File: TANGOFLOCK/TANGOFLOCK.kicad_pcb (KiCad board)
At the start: 2 copper layers, 31.8 x 31.8 mm, 7 parts, among them J1 USB-DEVICE-SHIELD, J2 USB-DEVICE-SHIELD, P2 ANTENNA, Q1 MOSFET_N

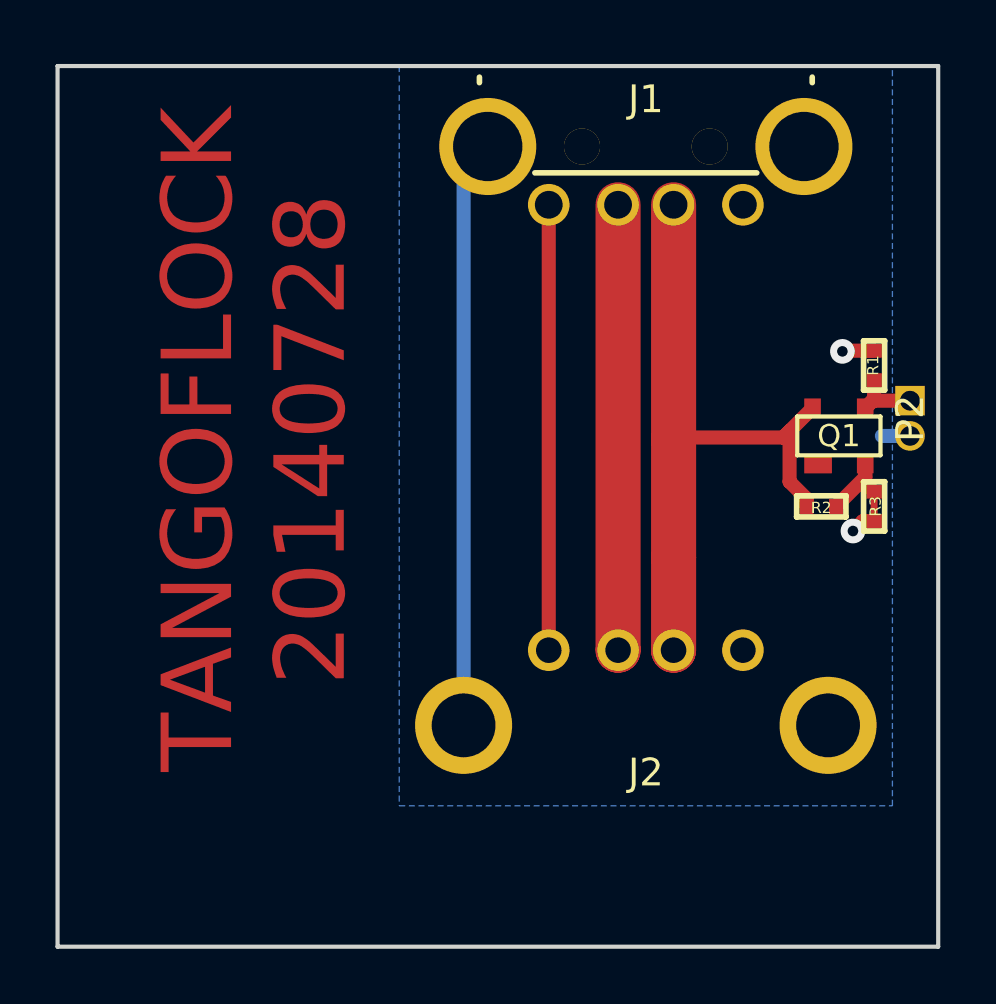
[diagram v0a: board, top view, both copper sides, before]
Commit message: simplified TANGOFLOCK
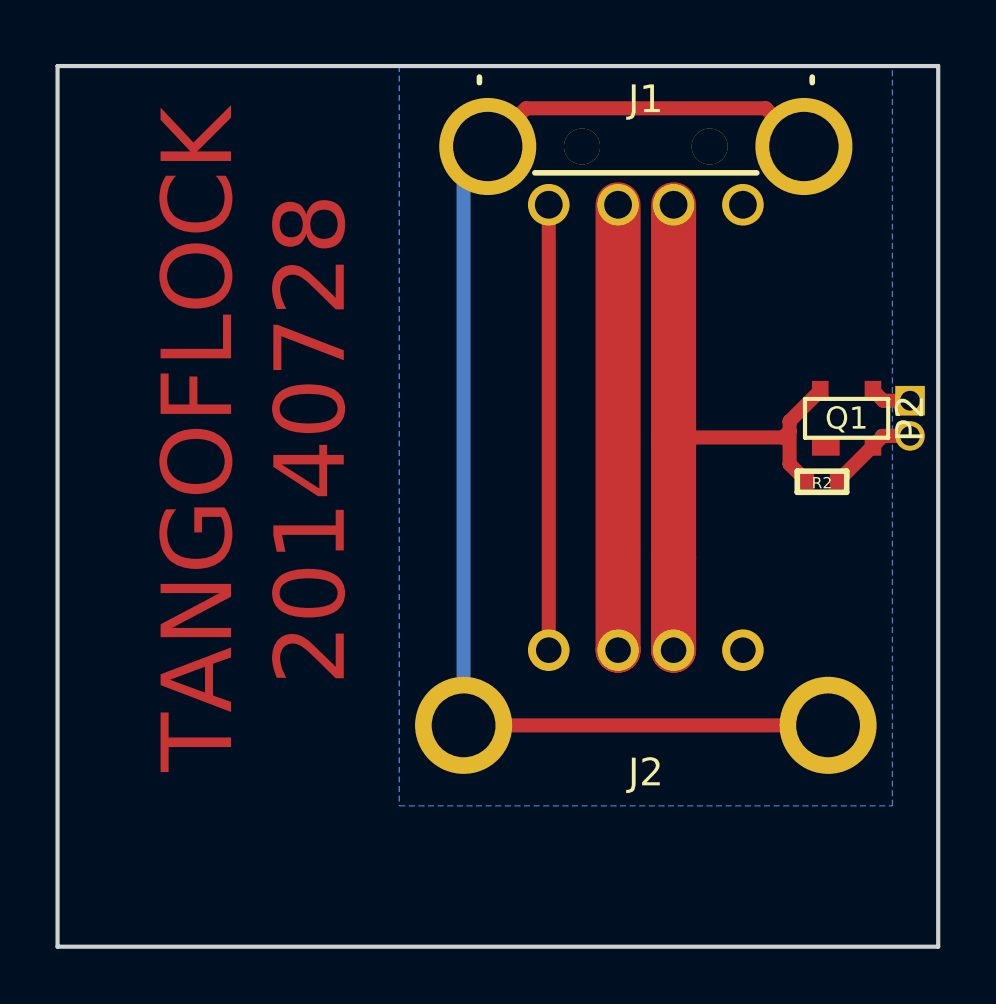
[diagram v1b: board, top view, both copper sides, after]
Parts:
- removed R1: DNP, GSG-0402
- removed R3: 0, GSG-0402-SHORT-10MIL
- moved R2 0.89 mm to (103.8, 91.2)
- moved Q1 0.69 mm to (104.6, 88.9)
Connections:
- Q1 pad S: /SOURCE -> GND
- R2 pad 2: /SOURCE -> GND
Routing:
- net /SHIELD: track 21.2 -> 46.9 mm
- net /SOURCE: track 3.11 -> 0.00 mm
- net /DRAIN: track 3.28 -> 1.49 mm
- net GND: track 3.08 -> 4.34 mm, vias 2 -> 0
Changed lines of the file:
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@@
 (kicad_pcb (version 3) (host pcbnew "(2012-nov-02)-stable")
   (general
-    (links 16)
-    (no_connects 2)
+    (links 13)
+    (no_connects 0)
     (area 69.115215 75.7468 108.202355 108.025001)
     (thickness 1.6)
     (drawings 6)
-    (tracks 40)
+    (tracks 34)
     (zones 0)
-    (modules 7)
-    (nets 8)
+    (modules 5)
+    (nets 7)
   )
   (page A3)
@@
   (net 2 /GATE)
   (net 3 /SHIELD)
-  (net 4 /SOURCE)
-  (net 5 GND)
+  (net 4 GND)
+  (net 5 N-000001)
   (net 6 N-000002)
-  (net 7 N-000003)
   (net_class Default "This is the default net class."
     (clearance 0.2032)
@@
     (add_net /GATE)
     (add_net /SHIELD)
-    (add_net /SOURCE)
     (add_net GND)
+    (add_net N-000001)
     (add_net N-000002)
-    (add_net N-000003)
   )
   (module GSG-0402 (layer F.Cu)
-    (at 103.7336 92.075)
+    (at 103.759 91.186)
     (solder_mask_margin 0.1016)
     (fp_text reference R2 (at 0 0.0508) (layer F.SilkS)
@@
     (pad 2 smd rect (at 0.5334 0) (size 0.508 0.5588)
       (layers F.Cu F.Paste F.Mask)
-      (net 4 /SOURCE)
+      (net 4 GND)
       (solder_mask_margin 0.1016)
     )
@@
     )
   )
-  (module GSG-0402 (layer F.Cu)
-    (at 105.6386 86.995 90)
-    (solder_mask_margin 0.1016)
-    (fp_text reference R1 (at 0 -0.037 90) (layer F.SilkS)
-      (effects (font (size 0.4064 0.4064) (thickness 0.1016)))
-    )
-    (fp_text value DNP (at 0 0.0508 90) (layer F.SilkS) hide
-      (effects (font (size 0.4064 0.4064) (thickness 0.1016)))
-    )
-    (fp_line (start 0.889 -0.381) (end 0.889 0.381) (layer F.SilkS) (width 0.2032))
-    (fp_line (start 0.889 0.381) (end -0.889 0.381) (layer F.SilkS) (width 0.2032))
-    (fp_line (start -0.889 0.381) (end -0.889 -0.381) (layer F.SilkS) (width 0.2032))
-    (fp_line (start -0.889 -0.381) (end 0.889 -0.381) (layer F.SilkS) (width 0.2032))
-    (pad 2 smd rect (at 0.5334 0 90) (size 0.508 0.5588)
-      (layers F.Cu F.Paste F.Mask)
-      (net 5 GND)
-      (solder_mask_margin 0.1016)
-    )
-    (pad 1 smd rect (at -0.5334 0 90) (size 0.508 0.5588)
-      (layers F.Cu F.Paste F.Mask)
-      (net 1 /DRAIN)
-      (die_length -2147.483648)
-      (solder_mask_margin 0.1016)
-    )
-  )
   (module GSG-50MIL-HEADER-1x2-TH (layer F.Cu)
     (at 106.934 88.9 270)
@@
     (pad 2 thru_hole circle (at 0.635 0 270) (size 1.0668 1.0668) (drill 0.7112)
       (layers *.Cu *.Mask)
-      (net 5 GND)
-    )
-  )
-  (module GSG-0402-SHORT-10MIL (layer F.Cu)
-    (at 105.6386 92.075 90)
-    (solder_mask_margin 0.1016)
-    (fp_text reference R3 (at 0 0.0508 90) (layer F.SilkS)
-      (effects (font (size 0.4064 0.4064) (thickness 0.1016)))
-    )
-    (fp_text value 0 (at 0 0.0508 90) (layer F.SilkS) hide
-      (effects (font (size 0.4064 0.4064) (thickness 0.1016)))
-    )
-    (fp_line (start 0.889 -0.381) (end 0.889 0.381) (layer F.SilkS) (width 0.2032))
-    (fp_line (start 0.889 0.381) (end -0.889 0.381) (layer F.SilkS) (width 0.2032))
-    (fp_line (start -0.889 0.381) (end -0.889 -0.381) (layer F.SilkS) (width 0.2032))
-    (fp_line (start -0.889 -0.381) (end 0.889 -0.381) (layer F.SilkS) (width 0.2032))
-    (pad 2 smd rect (at 0.5334 0 90) (size 0.508 0.5588)
-      (layers F.Cu F.Mask)
-      (net 4 /SOURCE)
-      (solder_mask_margin 0.1016)
-    )
-    (pad 1 smd rect (at -0.5334 0 90) (size 0.508 0.5588)
-      (layers F.Cu F.Mask)
-      (net 5 GND)
-      (die_length -2147.483648)
-      (solder_mask_margin 0.1016)
-    )
-    (pad "" smd rect (at 0 0 90) (size 0.762 0.254)
-      (layers F.Cu F.Mask)
+      (net 4 GND)
     )
   )
   (module GSG-SOT143B-GDS (layer F.Cu)
-    (at 104.3686 89.535)
+    (at 104.648 88.9)
     (fp_text reference Q1 (at 0 0) (layer F.SilkS)
       (effects (font (size 0.8 0.8) (thickness 0.15)))
@@
     (pad S smd rect (at 0.95 1) (size 0.6 0.7)
       (layers F.Cu F.Paste F.Mask)
-      (net 4 /SOURCE)
+      (net 4 GND)
     )
     (pad D smd rect (at 0.95 -1) (size 0.6 0.7)
@@
     (pad 2 thru_hole circle (at 1.00076 -5.00126 180) (size 1.50114 1.50114) (drill 1.00076)
       (layers *.Cu *.Mask F.SilkS)
-      (net 7 N-000003)
+      (net 5 N-000001)
     )
     (pad 3 thru_hole circle (at -1.00076 -5.00126 180) (size 1.50114 1.50114) (drill 1.00076)
@@
     (pad 4 thru_hole circle (at -3.50012 -5.00126 180) (size 1.50114 1.50114) (drill 1.00076)
       (layers *.Cu *.Mask F.SilkS)
-      (net 5 GND)
+      (net 4 GND)
     )
     (pad "" thru_hole circle (at 2.30124 -2.90068 180) (size 1.30048 1.30048) (drill 1.30048)
@@
     (pad 4 thru_hole circle (at 3.5 -5.61) (size 1.5 1.5) (drill 0.92)
       (layers *.Cu *.Mask F.SilkS)
-      (net 5 GND)
+      (net 4 GND)
     )
     (pad 3 thru_hole circle (at 1 -5.61) (size 1.5 1.5) (drill 0.92)
@@
     (pad 2 thru_hole circle (at -1 -5.61) (size 1.5 1.5) (drill 0.92)
       (layers *.Cu *.Mask F.SilkS)
-      (net 7 N-000003)
+      (net 5 N-000001)
     )
     (pad 1 thru_hole circle (at -3.5 -5.61) (size 1.5 1.5) (drill 0.92)
@@
     (effects (font (size 2.54 2.54) (thickness 0.381)))
   )
-  (segment (start 106.934 88.265) (end 105.5886 88.265) (width 0.508) (layer F.Cu) (net 1))
-  (segment (start 105.5886 88.265) (end 105.3186 88.535) (width 0.508) (layer F.Cu) (net 1))
-  (segment (start 105.6386 87.5284) (end 105.6386 88.265) (width 0.508) (layer F.Cu) (net 1))
-  (segment (start 105.6386 88.265) (end 105.5886 88.265) (width 0.508) (layer F.Cu) (net 1))
-  (segment (start 105.5886 88.265) (end 105.3186 88.535) (width 0.508) (layer F.Cu) (net 1))
-  (segment (start 105.5886 88.265) (end 105.3186 88.535) (width 0.508) (layer F.Cu) (net 1))
+  (segment (start 106.934 88.265) (end 105.963 88.265) (width 0.508) (layer F.Cu) (net 1))
+  (segment (start 105.963 88.265) (end 105.598 87.9) (width 0.508) (layer F.Cu) (net 1))
+  (segment (start 102.5906 89.363) (end 102.5906 90.551) (width 0.508) (layer F.Cu) (net 2))
+  (segment (start 102.5906 90.551) (end 103.2256 91.186) (width 0.508) (layer F.Cu) (net 2) (status 800000))
+  (segment (start 102.5906 89.363) (end 102.5906 89.0074) (width 0.508) (layer F.Cu) (net 2))
+  (segment (start 102.5906 89.0074) (end 103.698 87.9) (width 0.508) (layer F.Cu) (net 2))
   (segment (start 102.362 89.5916) (end 98.40976 89.5916) (width 0.508) (layer F.Cu) (net 2))
   (segment (start 98.298 89.662) (end 98.40976 89.662) (width 0.508) (layer F.Cu) (net 2))
@@
   (segment (start 98.40976 93.9292) (end 98.40976 97.25924) (width 1.6256) (layer F.Cu) (net 2))
   (segment (start 98.40976 97.25924) (end 98.409 97.26) (width 1.6256) (layer F.Cu) (net 2))
-  (segment (start 103.2002 92.075) (end 103.2002 91.7956) (width 0.508) (layer F.Cu) (net 2))
   (segment (start 102.5906 89.363) (end 102.362 89.5916) (width 0.508) (layer F.Cu) (net 2))
-  (segment (start 102.362 89.5916) (end 103.4186 88.535) (width 0.508) (layer F.Cu) (net 2))
-  (segment (start 102.5906 91.186) (end 102.5906 89.363) (width 0.508) (layer F.Cu) (net 2))
-  (segment (start 103.2002 91.7956) (end 102.5906 91.186) (width 0.508) (layer F.Cu) (net 2))
+  (segment (start 103.10876 79.10068) (end 101.73208 77.724) (width 0.508) (layer F.Cu) (net 3) (status 400000))
+  (segment (start 93.08592 77.724) (end 91.70924 79.10068) (width 0.508) (layer F.Cu) (net 3) (status 800000))
+  (segment (start 101.73208 77.724) (end 93.08592 77.724) (width 0.508) (layer F.Cu) (net 3))
+  (segment (start 103.979 99.97) (end 90.839 99.97) (width 0.508) (layer F.Cu) (net 3) (status C00000))
   (segment (start 90.839 99.97) (end 90.839 79.97092) (width 0.508) (layer B.Cu) (net 3))
   (segment (start 90.839 79.97092) (end 91.70924 79.10068) (width 0.508) (layer B.Cu) (net 3))
-  (segment (start 105.6386 91.5416) (end 105.3186 91.2216) (width 0.508) (layer F.Cu) (net 4))
-  (segment (start 105.3186 91.2216) (end 105.3186 90.535) (width 0.508) (layer F.Cu) (net 4))
-  (segment (start 104.267 92.075) (end 105.3186 91.0234) (width 0.508) (layer F.Cu) (net 4))
-  (segment (start 105.3186 91.0234) (end 105.3186 90.535) (width 0.508) (layer F.Cu) (net 4))
-  (segment (start 106.934 89.535) (end 105.918 89.535) (width 0.508) (layer B.Cu) (net 5))
-  (segment (start 105.6386 86.4616) (end 104.521 86.4616) (width 0.508) (layer F.Cu) (net 5))
-  (via (at 104.4956 86.487) (size 0.889) (layers F.Cu B.Cu) (net 5))
-  (segment (start 104.521 86.4616) (end 104.4956 86.487) (width 0.508) (layer F.Cu) (net 5))
-  (segment (start 105.6386 92.6084) (end 105.2322 92.6084) (width 0.508) (layer F.Cu) (net 5))
-  (via (at 104.8766 92.964) (size 0.889) (layers F.Cu B.Cu) (net 5))
-  (segment (start 105.2322 92.6084) (end 104.8766 92.964) (width 0.508) (layer F.Cu) (net 5))
+  (segment (start 104.2924 91.186) (end 104.312 91.186) (width 0.508) (layer F.Cu) (net 4) (status C00000))
+  (segment (start 104.312 91.186) (end 105.598 89.9) (width 0.508) (layer F.Cu) (net 4) (status C00000))
+  (segment (start 106.934 89.535) (end 105.963 89.535) (width 0.508) (layer F.Cu) (net 4))
+  (segment (start 105.963 89.535) (end 105.598 89.9) (width 0.508) (layer F.Cu) (net 4))
+  (segment (start 106.934 89.535) (end 105.918 89.535) (width 0.508) (layer B.Cu) (net 4))
+  (segment (start 96.40824 81.20126) (end 96.40824 97.25924) (width 1.6256) (layer F.Cu) (net 5))
+  (segment (start 96.40824 97.25924) (end 96.409 97.26) (width 1.6256) (layer F.Cu) (net 5))
   (segment (start 93.90888 97.25988) (end 93.909 97.26) (width 0.508) (layer F.Cu) (net 6))
   (segment (start 93.90888 81.20126) (end 93.90888 97.25988) (width 0.508) (layer F.Cu) (net 6))
-  (segment (start 96.40824 81.20126) (end 96.40824 97.25924) (width 1.6256) (layer F.Cu) (net 7))
-  (segment (start 96.40824 97.25924) (end 96.409 97.26) (width 1.6256) (layer F.Cu) (net 7))
-  (zone (net 5) (net_name GND) (layer B.Cu) (hatch edge 0.508)
+  (zone (net 4) (net_name GND) (layer B.Cu) (hatch edge 0.508)
     (connect_pads (clearance 0.254))
     (min_thickness 0.254)

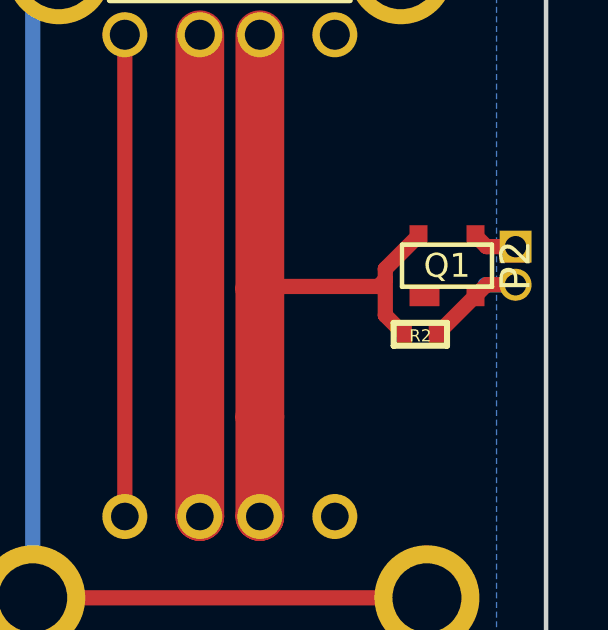
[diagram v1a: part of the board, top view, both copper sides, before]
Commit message: connected BSS83,215 substrate to source (previous workaround was solder blob)
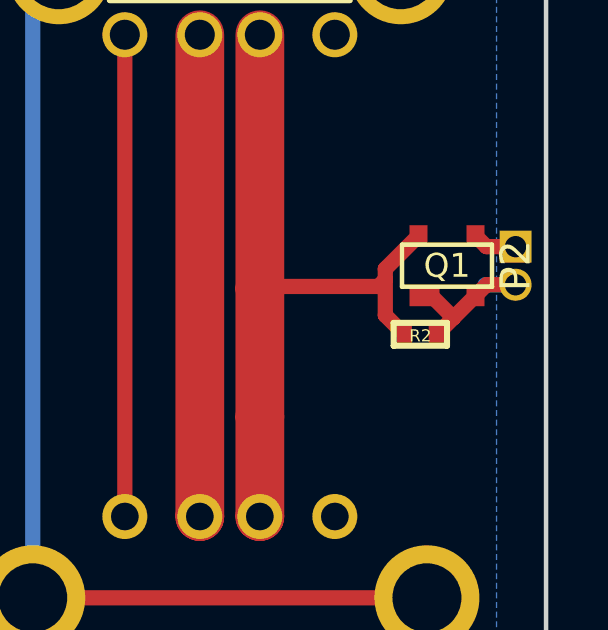
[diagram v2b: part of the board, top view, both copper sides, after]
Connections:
- Q1 pad B: (no net) -> GND
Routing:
- net GND: track 4.34 -> 5.61 mm
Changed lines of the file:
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@@
 (kicad_pcb (version 3) (host pcbnew "(2012-nov-02)-stable")
   (general
-    (links 13)
+    (links 14)
     (no_connects 0)
-    (area 69.115215 75.7468 108.202355 108.025001)
+    (area 69.115215 75.7468 108.481755 108.025001)
     (thickness 1.6)
     (drawings 6)
-    (tracks 34)
+    (tracks 37)
     (zones 0)
     (modules 5)
@@
     (pad B smd rect (at -0.75 1) (size 1 0.7)
       (layers F.Cu F.Paste F.Mask)
+      (net 4 GND)
     )
     (pad S smd rect (at 0.95 1) (size 0.6 0.7)
@@
     (pad 1 thru_hole circle (at 3.50012 -5.00126 180) (size 1.50114 1.50114) (drill 1.00076)
       (layers *.Cu *.Mask F.SilkS)
+      (net 5 N-000001)
+    )
+    (pad 2 thru_hole circle (at 1.00076 -5.00126 180) (size 1.50114 1.50114) (drill 1.00076)
+      (layers *.Cu *.Mask F.SilkS)
       (net 6 N-000002)
-    )
-    (pad 2 thru_hole circle (at 1.00076 -5.00126 180) (size 1.50114 1.50114) (drill 1.00076)
-      (layers *.Cu *.Mask F.SilkS)
-      (net 5 N-000001)
     )
     (pad 3 thru_hole circle (at -1.00076 -5.00126 180) (size 1.50114 1.50114) (drill 1.00076)
@@
     (pad 2 thru_hole circle (at -1 -5.61) (size 1.5 1.5) (drill 0.92)
       (layers *.Cu *.Mask F.SilkS)
+      (net 6 N-000002)
+    )
+    (pad 1 thru_hole circle (at -3.5 -5.61) (size 1.5 1.5) (drill 0.92)
+      (layers *.Cu *.Mask F.SilkS)
       (net 5 N-000001)
-    )
-    (pad 1 thru_hole circle (at -3.5 -5.61) (size 1.5 1.5) (drill 0.92)
-      (layers *.Cu *.Mask F.SilkS)
-      (net 6 N-000002)
     )
     (pad 5 thru_hole circle (at 6.57 -2.9) (size 3.5 3.5) (drill 2.3)
@@
   (segment (start 105.963 88.265) (end 105.598 87.9) (width 0.508) (layer F.Cu) (net 1))
   (segment (start 102.5906 89.363) (end 102.5906 90.551) (width 0.508) (layer F.Cu) (net 2))
-  (segment (start 102.5906 90.551) (end 103.2256 91.186) (width 0.508) (layer F.Cu) (net 2) (status 800000))
+  (segment (start 102.5906 90.551) (end 103.2256 91.186) (width 0.508) (layer F.Cu) (net 2))
   (segment (start 102.5906 89.363) (end 102.5906 89.0074) (width 0.508) (layer F.Cu) (net 2))
   (segment (start 102.5906 89.0074) (end 103.698 87.9) (width 0.508) (layer F.Cu) (net 2))
@@
   (segment (start 98.40976 97.25924) (end 98.409 97.26) (width 1.6256) (layer F.Cu) (net 2))
   (segment (start 102.5906 89.363) (end 102.362 89.5916) (width 0.508) (layer F.Cu) (net 2))
-  (segment (start 103.10876 79.10068) (end 101.73208 77.724) (width 0.508) (layer F.Cu) (net 3) (status 400000))
-  (segment (start 93.08592 77.724) (end 91.70924 79.10068) (width 0.508) (layer F.Cu) (net 3) (status 800000))
+  (segment (start 103.10876 79.10068) (end 101.73208 77.724) (width 0.508) (layer F.Cu) (net 3))
+  (segment (start 93.08592 77.724) (end 91.70924 79.10068) (width 0.508) (layer F.Cu) (net 3))
   (segment (start 101.73208 77.724) (end 93.08592 77.724) (width 0.508) (layer F.Cu) (net 3))
-  (segment (start 103.979 99.97) (end 90.839 99.97) (width 0.508) (layer F.Cu) (net 3) (status C00000))
+  (segment (start 103.979 99.97) (end 90.839 99.97) (width 0.508) (layer F.Cu) (net 3))
   (segment (start 90.839 99.97) (end 90.839 79.97092) (width 0.508) (layer B.Cu) (net 3))
   (segment (start 90.839 79.97092) (end 91.70924 79.10068) (width 0.508) (layer B.Cu) (net 3))
-  (segment (start 104.2924 91.186) (end 104.312 91.186) (width 0.508) (layer F.Cu) (net 4) (status C00000))
-  (segment (start 104.312 91.186) (end 105.598 89.9) (width 0.508) (layer F.Cu) (net 4) (status C00000))
+  (segment (start 103.898 89.9) (end 104.124 89.9) (width 0.508) (layer F.Cu) (net 4) (status C00000))
+  (segment (start 104.124 89.9) (end 104.861 90.637) (width 0.508) (layer F.Cu) (net 4) (status 400000))
+  (segment (start 104.2924 91.186) (end 104.312 91.186) (width 0.508) (layer F.Cu) (net 4))
+  (segment (start 104.312 91.186) (end 104.861 90.637) (width 0.508) (layer F.Cu) (net 4))
+  (segment (start 104.861 90.637) (end 105.598 89.9) (width 0.508) (layer F.Cu) (net 4))
   (segment (start 106.934 89.535) (end 105.963 89.535) (width 0.508) (layer F.Cu) (net 4))
   (segment (start 105.963 89.535) (end 105.598 89.9) (width 0.508) (layer F.Cu) (net 4))
   (segment (start 106.934 89.535) (end 105.918 89.535) (width 0.508) (layer B.Cu) (net 4))
-  (segment (start 96.40824 81.20126) (end 96.40824 97.25924) (width 1.6256) (layer F.Cu) (net 5))
-  (segment (start 96.40824 97.25924) (end 96.409 97.26) (width 1.6256) (layer F.Cu) (net 5))
-  (segment (start 93.90888 97.25988) (end 93.909 97.26) (width 0.508) (layer F.Cu) (net 6))
-  (segment (start 93.90888 81.20126) (end 93.90888 97.25988) (width 0.508) (layer F.Cu) (net 6))
+  (segment (start 93.90888 97.25988) (end 93.909 97.26) (width 0.508) (layer F.Cu) (net 5))
+  (segment (start 93.90888 81.20126) (end 93.90888 97.25988) (width 0.508) (layer F.Cu) (net 5))
+  (segment (start 96.40824 81.20126) (end 96.40824 97.25924) (width 1.6256) (layer F.Cu) (net 6))
+  (segment (start 96.40824 97.25924) (end 96.409 97.26) (width 1.6256) (layer F.Cu) (net 6))
   (zone (net 4) (net_name GND) (layer B.Cu) (hatch edge 0.508)
     (connect_pads (clearance 0.254))
